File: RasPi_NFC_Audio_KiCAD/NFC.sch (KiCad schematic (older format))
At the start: 30 parts

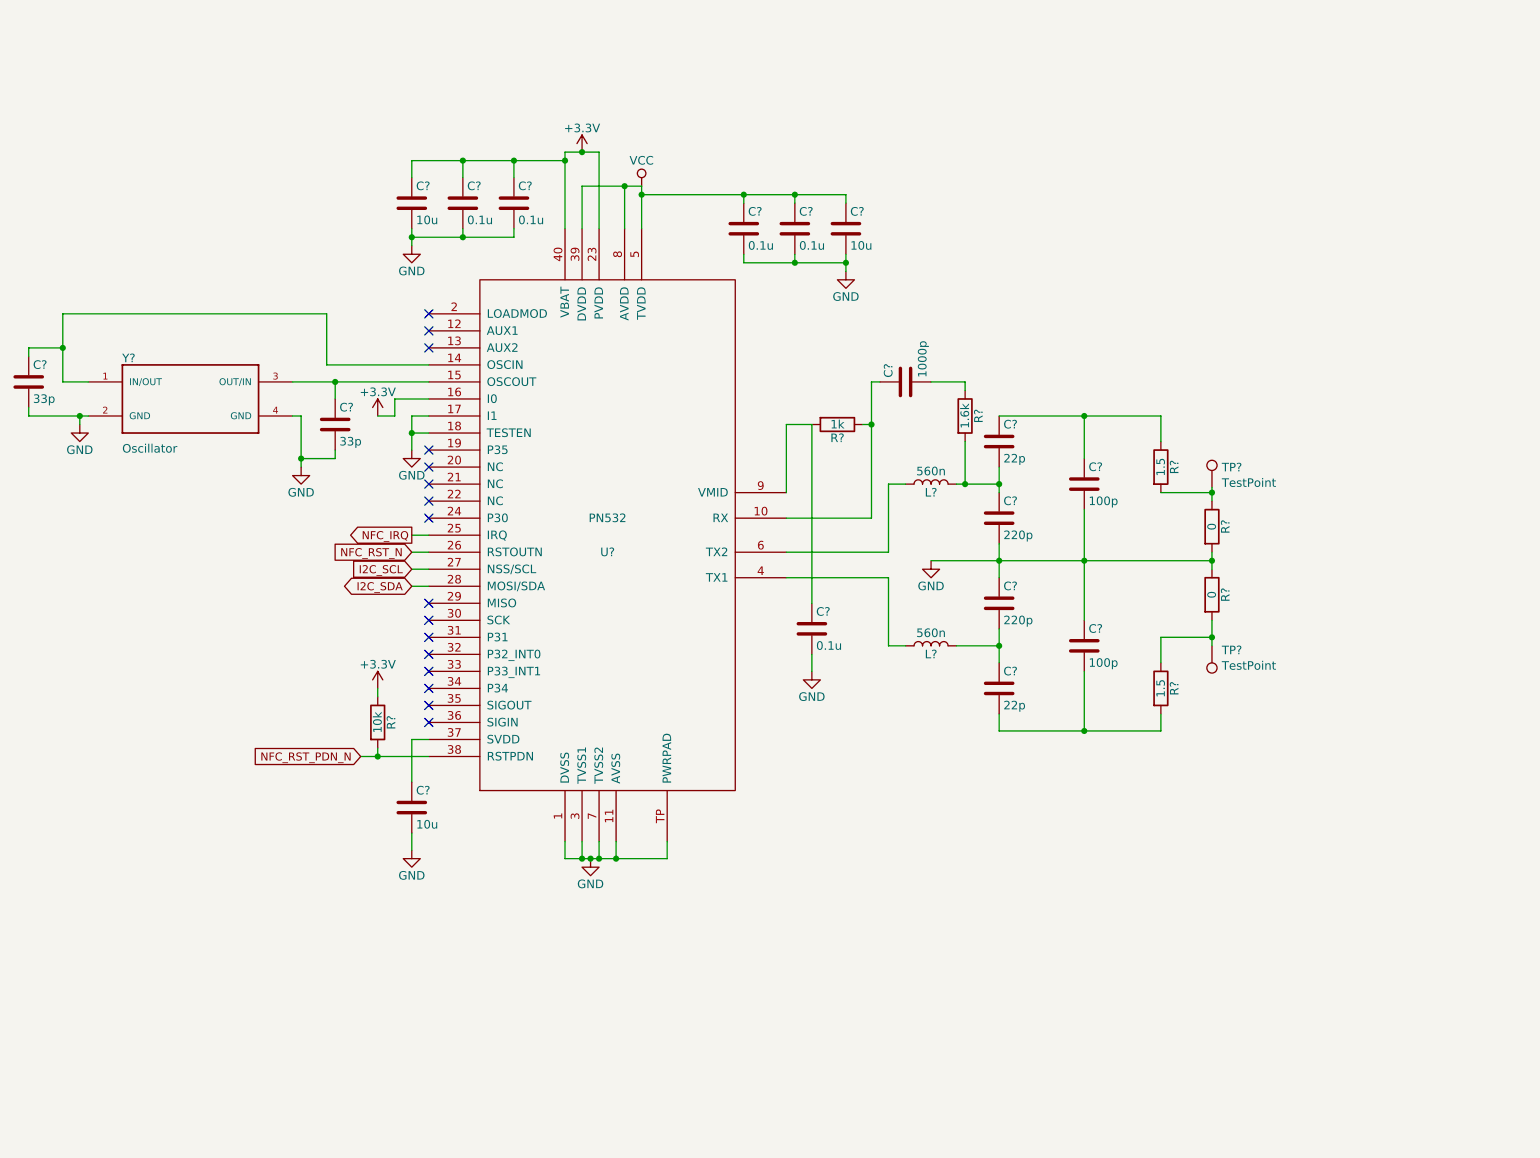
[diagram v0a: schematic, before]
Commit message: Added protocol selection jumpers
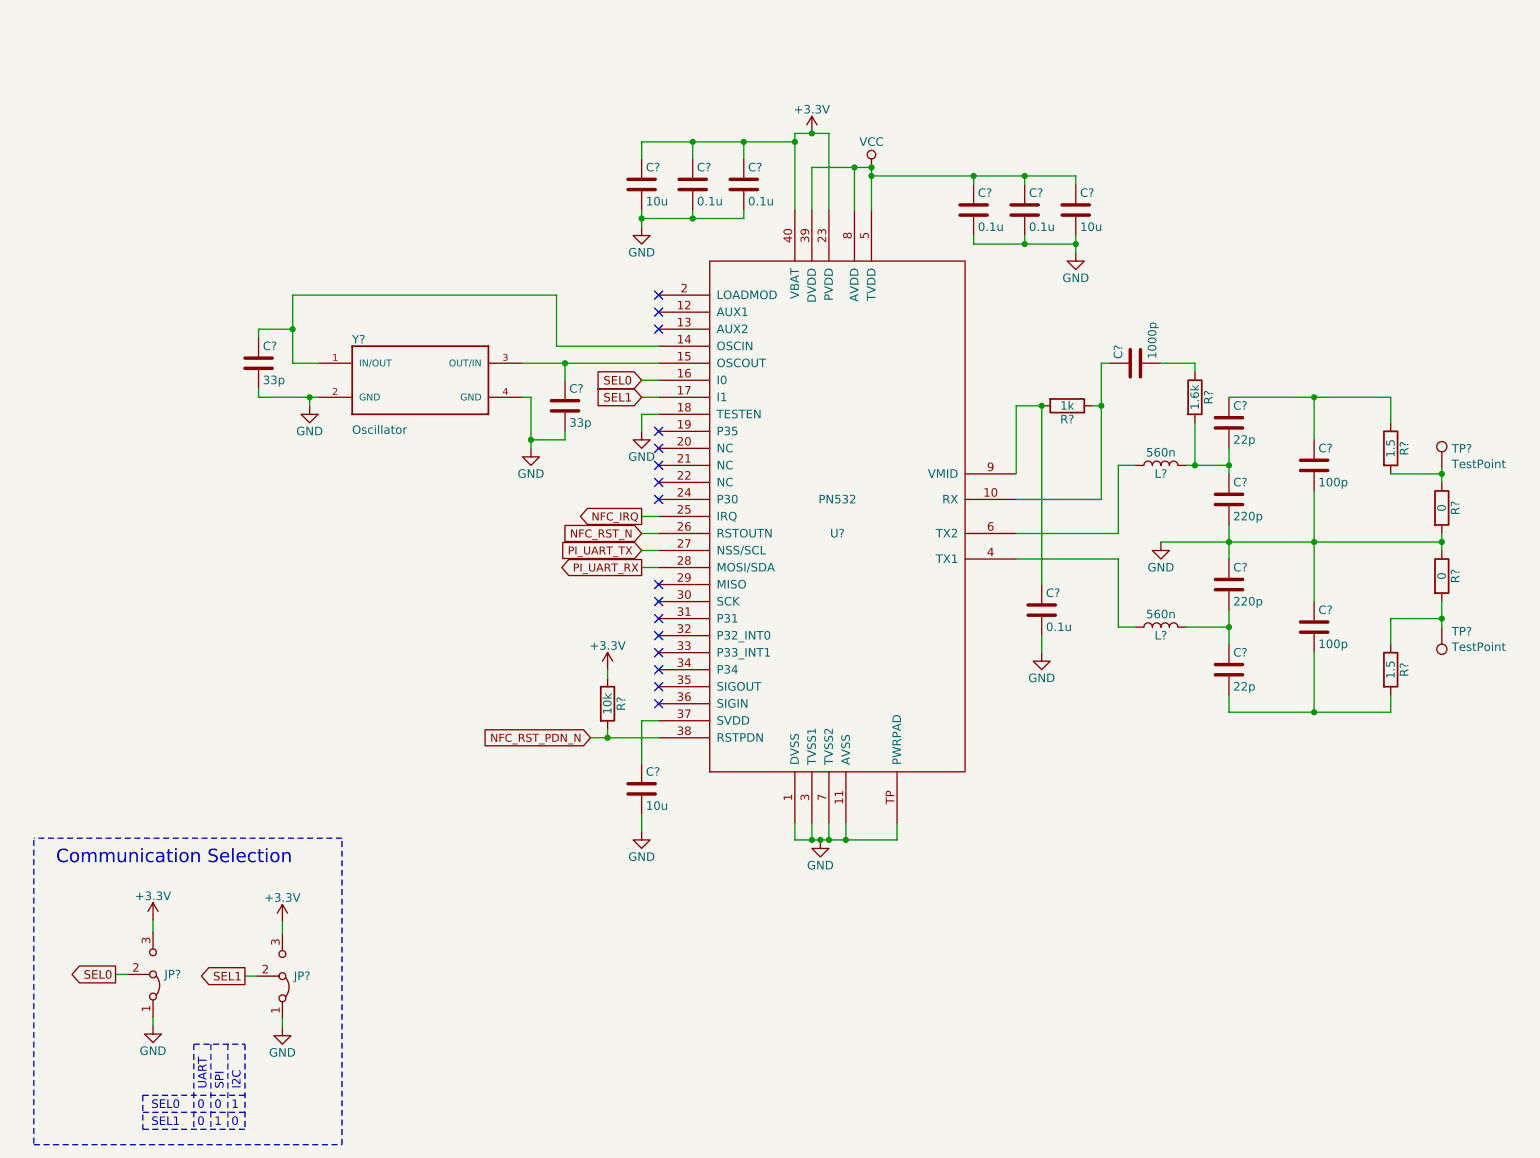
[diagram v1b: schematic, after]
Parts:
- added JP? (x2): Jumper_3_Bridged12, symbol Jumper:Jumper_3_Bridged12
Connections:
- net +3V3: now also JP?.3 (B), JP?.3 (B); no longer U?.16 (I0)
- net GND: now also JP?.1 (A), JP?.1 (A); no longer U?.17 (I1)
- net I2C_SCL renamed PI_UART_TX
- net I2C_SDA renamed PI_UART_RX
- new net SEL0: JP?.2 (C), U?.16 (I0)
- new net SEL1: JP?.2 (C), U?.17 (I1)
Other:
- note added: "0"
- note added: "1"
- note added: "Communication Selection"
- note added: "I2C"
- note added: "SEL0"
- note added: "SEL1"
- note added: "SPI"
- note added: "UART"
- moved on the sheet: C?, L?, R?, TP?, U?, Y?

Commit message: Schematic update
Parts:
- added C?: 0.1u, Capacitors_SMD:C_0402, symbol Device:C
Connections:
- net +3V3: no longer R?.1, U?.23 (PVDD)
- net GND: now also C?.2
- net NFC_RST_N renamed NFC_RSTOUT_N
- new net VCOM: C?.1, R?.1, U?.23 (PVDD)
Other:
- moved on the sheet: C?
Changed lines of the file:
@@
 $EndComp
 $Comp
-L power:+3.3V #PWR?
+L power:+3.3V #PWR0116
 U 1 1 5ACE3D82
-P 6250 1490
-F 0 "#PWR?" H 6250 1340 50  0001 C CNN
-F 1 "+3.3V" H 6250 1630 50  0000 C CNN
-F 2 "" H 6250 1490 50  0001 C CNN
-F 3 "" H 6250 1490 50  0001 C CNN
-	1    6250 1490
-	1    0    0    -1
-$EndComp
-$Comp
-L power:GND #PWR?
+P 6150 1050
+F 0 "#PWR0116" H 6150 900 50  0001 C CNN
+F 1 "+3.3V" H 6150 1190 50  0000 C CNN
+F 2 "" H 6150 1050 50  0001 C CNN
+F 3 "" H 6150 1050 50  0001 C CNN
+	1    6150 1050
+	1    0    0    -1
+$EndComp
+$Comp
+L power:GND #PWR0117
 U 1 1 5ACE3D89
 P 6300 5640
-F 0 "#PWR?" H 6300 5390 50  0001 C CNN
+F 0 "#PWR0117" H 6300 5390 50  0001 C CNN
 F 1 "GND" H 6300 5490 50  0000 C CNN
 F 2 "" H 6300 5640 50  0001 C CNN
@@
 $EndComp
 Wire Wire Line
-	6350 1490 6350 1940
-Wire Wire Line
-	6150 1490 6250 1490
-Wire Wire Line
-	6150 1490 6150 1540
-Connection ~ 6250 1490
-$Comp
-L power:VCC #PWR?
+	6150 1050 6150 1100
+$Comp
+L power:VCC #PWR0118
 U 1 1 5ACE49E2
 P 6600 1690
-F 0 "#PWR?" H 6600 1540 50  0001 C CNN
+F 0 "#PWR0118" H 6600 1540 50  0001 C CNN
 F 1 "VCC" H 6600 1840 50  0000 C CNN
 F 2 "" H 6600 1690 50  0001 C CNN
@@
 $EndComp
 $Comp
-L power:GND #PWR?
+L power:GND #PWR0119
 U 1 1 5ACEB7BE
 P 8300 3890
-F 0 "#PWR?" H 8300 3640 50  0001 C CNN
+F 0 "#PWR0119" H 8300 3640 50  0001 C CNN
 F 1 "GND" H 8300 3740 50  0000 C CNN
 F 2 "" H 8300 3890 50  0001 C CNN
@@
 	7600 3090 7450 3090
 $Comp
-L power:GND #PWR?
+L power:GND #PWR0120
 U 1 1 5ACEC797
 P 7600 4540
-F 0 "#PWR?" H 7600 4290 50  0001 C CNN
+F 0 "#PWR0120" H 7600 4290 50  0001 C CNN
 F 1 "GND" H 7600 4390 50  0000 C CNN
 F 2 "" H 7600 4540 50  0001 C CNN
@@
 	4550 2840 4800 2840
 $Comp
-L power:GND #PWR?
+L power:GND #PWR0121
 U 1 1 5ACECF73
 P 4600 3340
-F 0 "#PWR?" H 4600 3090 50  0001 C CNN
+F 0 "#PWR0121" H 4600 3090 50  0001 C CNN
 F 1 "GND" H 4600 3190 50  0000 C CNN
 F 2 "" H 4600 3340 50  0001 C CNN
@@
 	4600 3040 4600 3290
 $Comp
-L power:GND #PWR?
+L power:GND #PWR0122
 U 1 1 5ACED04D
 P 3300 3090
-F 0 "#PWR?" H 3300 2840 50  0001 C CNN
+F 0 "#PWR0122" H 3300 2840 50  0001 C CNN
 F 1 "GND" H 3300 2940 50  0000 C CNN
 F 2 "" H 3300 3090 50  0001 C CNN
@@
 Connection ~ 4800 2840
 $Comp
-L power:GND #PWR?
+L power:GND #PWR0123
 U 1 1 5ACED8D4
 P 5250 3240
-F 0 "#PWR?" H 5250 2990 50  0001 C CNN
+F 0 "#PWR0123" H 5250 2990 50  0001 C CNN
 F 1 "GND" H 5250 3090 50  0000 C CNN
 F 2 "" H 5250 3240 50  0001 C CNN
@@
 Wire Wire Line
 	5350 2940 5250 2940
-Text GLabel 5250 3840 0    47   Input ~ 0
-NFC_RST_N
+Text GLabel 5250 3840 0    47   Output ~ 0
+NFC_RSTOUT_N
 Wire Wire Line
 	5250 3840 5350 3840
@@
 	1    0    0    -1
 $EndComp
-$Comp
-L power:+3.3V #PWR?
-U 1 1 5ACEF2AA
-P 5050 4640
-F 0 "#PWR?" H 5050 4490 50  0001 C CNN
-F 1 "+3.3V" H 5050 4780 50  0000 C CNN
-F 2 "" H 5050 4640 50  0001 C CNN
-F 3 "" H 5050 4640 50  0001 C CNN
-	1    5050 4640
-	1    0    0    -1
-$EndComp
 Wire Wire Line
 	5050 4640 5050 4690
@@
 L Device:C C?
 U 1 1 5ACF004D
-P 5550 1790
-F 0 "C?" H 5575 1890 50  0000 L CNN
-F 1 "0.1u" H 5575 1690 50  0000 L CNN
-F 2 "Capacitors_SMD:C_0402" H 5588 1640 50  0001 C CNN
-F 3 "" H 5550 1790 50  0001 C CNN
-	1    5550 1790
+P 5550 1350
+F 0 "C?" H 5575 1450 50  0000 L CNN
+F 1 "0.1u" H 5575 1250 50  0000 L CNN
+F 2 "Capacitors_SMD:C_0402" H 5588 1200 50  0001 C CNN
+F 3 "" H 5550 1350 50  0001 C CNN
+	1    5550 1350
 	1    0    0    -1
 $EndComp
@@
 L Device:C C?
 U 1 1 5ACF00B0
-P 5850 1790
-F 0 "C?" H 5875 1890 50  0000 L CNN
-F 1 "0.1u" H 5875 1690 50  0000 L CNN
-F 2 "Capacitors_SMD:C_0402" H 5888 1640 50  0001 C CNN
-F 3 "" H 5850 1790 50  0001 C CNN
-	1    5850 1790
+P 5850 1350
+F 0 "C?" H 5875 1450 50  0000 L CNN
+F 1 "0.1u" H 5875 1250 50  0000 L CNN
+F 2 "Capacitors_SMD:C_0402" H 5888 1200 50  0001 C CNN
+F 3 "" H 5850 1350 50  0001 C CNN
+	1    5850 1350
 	1    0    0    -1
 $EndComp
@@
 Connection ~ 7200 1740
 Wire Wire Line
-	5850 1540 5850 1640
+	5850 1100 5850 1200
 Connection ~ 7500 1740
 Wire Wire Line
@@
 	7800 1740 7800 1790
 Wire Wire Line
-	5250 1540 5550 1540
-Connection ~ 6150 1540
-Wire Wire Line
-	5550 1640 5550 1540
-Connection ~ 5850 1540
+	5250 1100 5550 1100
+Connection ~ 6150 1100
+Wire Wire Line
+	5550 1200 5550 1100
+Connection ~ 5850 1100
 $Comp
 L Device:C C?
 U 1 1 5ACF095C
-P 5250 1790
-F 0 "C?" H 5275 1890 50  0000 L CNN
-F 1 "10u" H 5275 1690 50  0000 L CNN
-F 2 "Capacitors_SMD:C_0603_HandSoldering" H 5288 1640 50  0001 C CNN
-F 3 "" H 5250 1790 50  0001 C CNN
-	1    5250 1790
-	1    0    0    -1
-$EndComp
-Wire Wire Line
-	5250 1640 5250 1540
-Connection ~ 5550 1540
-$Comp
-L power:GND #PWR?
+P 5250 1350
+F 0 "C?" H 5275 1450 50  0000 L CNN
+F 1 "10u" H 5275 1250 50  0000 L CNN
+F 2 "Capacitors_SMD:C_0603_HandSoldering" H 5288 1200 50  0001 C CNN
+F 3 "" H 5250 1350 50  0001 C CNN
+	1    5250 1350
+	1    0    0    -1
+$EndComp
+Wire Wire Line
+	5250 1200 5250 1100
+Connection ~ 5550 1100
+$Comp
+L power:GND #PWR0124
 U 1 1 5ACF0B0F
-P 5250 2040
-F 0 "#PWR?" H 5250 1790 50  0001 C CNN
-F 1 "GND" H 5250 1890 50  0000 C CNN
-F 2 "" H 5250 2040 50  0001 C CNN
-F 3 "" H 5250 2040 50  0001 C CNN
-	1    5250 2040
-	1    0    0    -1
-$EndComp
-$Comp
-L power:GND #PWR?
+P 5250 1690
+F 0 "#PWR0124" H 5250 1440 50  0001 C CNN
+F 1 "GND" H 5250 1540 50  0000 C CNN
+F 2 "" H 5250 1690 50  0001 C CNN
+F 3 "" H 5250 1690 50  0001 C CNN
+	1    5250 1690
+	1    0    0    -1
+$EndComp
+$Comp
+L power:GND #PWR0125
 U 1 1 5ACF0B6E
 P 7800 2190
-F 0 "#PWR?" H 7800 1940 50  0001 C CNN
+F 0 "#PWR0125" H 7800 1940 50  0001 C CNN
 F 1 "GND" H 7800 2040 50  0000 C CNN
 F 2 "" H 7800 2190 50  0001 C CNN
@@
 Connection ~ 7500 2140
 Wire Wire Line
-	5250 1940 5250 1990
-Wire Wire Line
-	5850 1990 5850 1940
-Wire Wire Line
-	5250 1990 5550 1990
-Connection ~ 5250 1990
-Wire Wire Line
-	5550 1940 5550 1990
-Connection ~ 5550 1990
+	5250 1500 5250 1640
+Wire Wire Line
+	5850 1640 5850 1500
+Wire Wire Line
+	5250 1640 5550 1640
+Connection ~ 5250 1640
+Wire Wire Line
+	5550 1500 5550 1640
+Connection ~ 5550 1640
 $Comp
 L Device:C C?
@@
 $EndComp
 $Comp
-L power:GND #PWR?
+L power:GND #PWR0126
 U 1 1 5ACF12FD
 P 5250 5590
-F 0 "#PWR?" H 5250 5340 50  0001 C CNN
+F 0 "#PWR0126" H 5250 5340 50  0001 C CNN
 F 1 "GND" H 5250 5440 50  0000 C CNN
 F 2 "" H 5250 5590 50  0001 C CNN
@@
 	7200 2140 7500 2140
 Wire Wire Line
-	6250 1490 6350 1490
-Wire Wire Line
 	6500 1690 6600 1690
 Wire Wire Line
@@
 	7500 1740 7800 1740
 Wire Wire Line
-	6150 1540 6150 1940
-Wire Wire Line
-	5850 1540 6150 1540
-Wire Wire Line
-	5550 1540 5850 1540
+	6150 1100 6150 1940
+Wire Wire Line
+	5850 1100 6150 1100
+Wire Wire Line
+	5550 1100 5850 1100
 Wire Wire Line
 	7800 2140 7800 2190
@@
 	7500 2140 7800 2140
 Wire Wire Line
-	5250 1990 5250 2040
-Wire Wire Line
-	5550 1990 5850 1990
+	5250 1640 5250 1690
+Wire Wire Line
+	5550 1640 5850 1640
 Wire Wire Line
 	9950 4340 9950 4390
@@
 SEL0
 $Comp
-L power:GND #PWR?
+L power:GND #PWR0127
 U 1 1 5E1B7458
 P 2380 6730
-F 0 "#PWR?" H 2380 6480 50  0001 C CNN
+F 0 "#PWR0127" H 2380 6480 50  0001 C CNN
 F 1 "GND" H 2380 6580 50  0000 C CNN
 F 2 "" H 2380 6730 50  0001 C CNN
@@
 $EndComp
 $Comp
-L power:+3.3V #PWR?
+L power:+3.3V #PWR0128
 U 1 1 5E1B7781
 P 2380 6110
-F 0 "#PWR?" H 2380 5960 50  0001 C CNN
+F 0 "#PWR0128" H 2380 5960 50  0001 C CNN
 F 1 "+3.3V" H 2380 6250 50  0000 C CNN
 F 2 "" H 2380 6110 50  0001 C CNN
@@
 SEL1
 $Comp
-L power:GND #PWR?
+L power:GND #PWR0129
 U 1 1 5E1D407F
 P 3140 6740
-F 0 "#PWR?" H 3140 6490 50  0001 C CNN
+F 0 "#PWR0129" H 3140 6490 50  0001 C CNN
 F 1 "GND" H 3140 6590 50  0000 C CNN
 F 2 "" H 3140 6740 50  0001 C CNN
@@
 $EndComp
 $Comp
-L power:+3.3V #PWR?
+L power:+3.3V #PWR0130
 U 1 1 5E1D4089
 P 3140 6120
-F 0 "#PWR?" H 3140 5970 50  0001 C CNN
+F 0 "#PWR0130" H 3140 5970 50  0001 C CNN
 F 1 "+3.3V" H 3140 6260 50  0000 C CNN
 F 2 "" H 3140 6120 50  0001 C CNN
@@
 Connection ~ 6600 1690
 Connection ~ 7600 3090
+$Comp
+L power:VCOM #PWR0131
+U 1 1 5E1E297F
+P 6350 1010
+F 0 "#PWR0131" H 6350 860 50  0001 C CNN
+F 1 "VCOM" H 6367 1183 50  0000 C CNN
+F 2 "" H 6350 1010 50  0001 C CNN
+F 3 "" H 6350 1010 50  0001 C CNN
+	1    6350 1010
+	1    0    0    -1
+$EndComp
+Wire Wire Line
+	6350 1010 6350 1040
+$Comp
+L Device:C C?
+U 1 1 5E208532
+P 6810 1200
+F 0 "C?" H 6835 1300 50  0000 L CNN
+F 1 "0.1u" H 6835 1100 50  0000 L CNN
+F 2 "Capacitors_SMD:C_0402" H 6848 1050 50  0001 C CNN
+F 3 "" H 6810 1200 50  0001 C CNN
+	1    6810 1200
+	1    0    0    -1
+$EndComp
+Wire Wire Line
+	6350 1040 6810 1040
+Connection ~ 6350 1040
+Wire Wire Line
+	6350 1040 6350 1940
+Wire Wire Line
+	6810 1050 6810 1040
+$Comp
+L power:GND #PWR0132
+U 1 1 5E219318
+P 6810 1410
+F 0 "#PWR0132" H 6810 1160 50  0001 C CNN
+F 1 "GND" H 6810 1260 50  0000 C CNN
+F 2 "" H 6810 1410 50  0001 C CNN
+F 3 "" H 6810 1410 50  0001 C CNN
+	1    6810 1410
+	1    0    0    -1
+$EndComp
+Wire Wire Line
+	6810 1410 6810 1350
+$Comp
+L power:VCOM #PWR0133
+U 1 1 5E30C600
+P 5050 4640
+F 0 "#PWR0133" H 5050 4490 50  0001 C CNN
+F 1 "VCOM" H 5067 4813 50  0000 C CNN
+F 2 "" H 5050 4640 50  0001 C CNN
+F 3 "" H 5050 4640 50  0001 C CNN
+	1    5050 4640
+	1    0    0    -1
+$EndComp
 $EndSCHEMATC

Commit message: Schematic Updates
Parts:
- C? (x3): DigiKey (none) -> 1276-1119-1-ND; Part # (none) -> CL10A106MQ8NNNC
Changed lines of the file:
@@
 F 2 "Capacitors_SMD:C_0603_HandSoldering" H 7838 1790 50  0001 C CNN
 F 3 "" H 7800 1940 50  0001 C CNN
+F 4 "CL10A106MQ8NNNC" H 7800 1940 50  0001 C CNN "Part #"
+F 5 "1276-1119-1-ND" H 7800 1940 50  0001 C CNN "DigiKey"
 	1    7800 1940
 	1    0    0    -1
@@
 F 2 "Capacitors_SMD:C_0603_HandSoldering" H 5288 1200 50  0001 C CNN
 F 3 "" H 5250 1350 50  0001 C CNN
+F 4 "CL10A106MQ8NNNC" H 5250 1350 50  0001 C CNN "Part #"
+F 5 "1276-1119-1-ND" H 5250 1350 50  0001 C CNN "DigiKey"
 	1    5250 1350
 	1    0    0    -1
@@
 F 2 "Capacitors_SMD:C_0603_HandSoldering" H 5288 5190 50  0001 C CNN
 F 3 "" H 5250 5340 50  0001 C CNN
+F 4 "CL10A106MQ8NNNC" H 5250 5340 50  0001 C CNN "Part #"
+F 5 "1276-1119-1-ND" H 5250 5340 50  0001 C CNN "DigiKey"
 	1    5250 5340
 	1    0    0    -1
